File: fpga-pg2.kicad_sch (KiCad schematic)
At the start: 1 part, among them U1 XC7A15T-FTG256

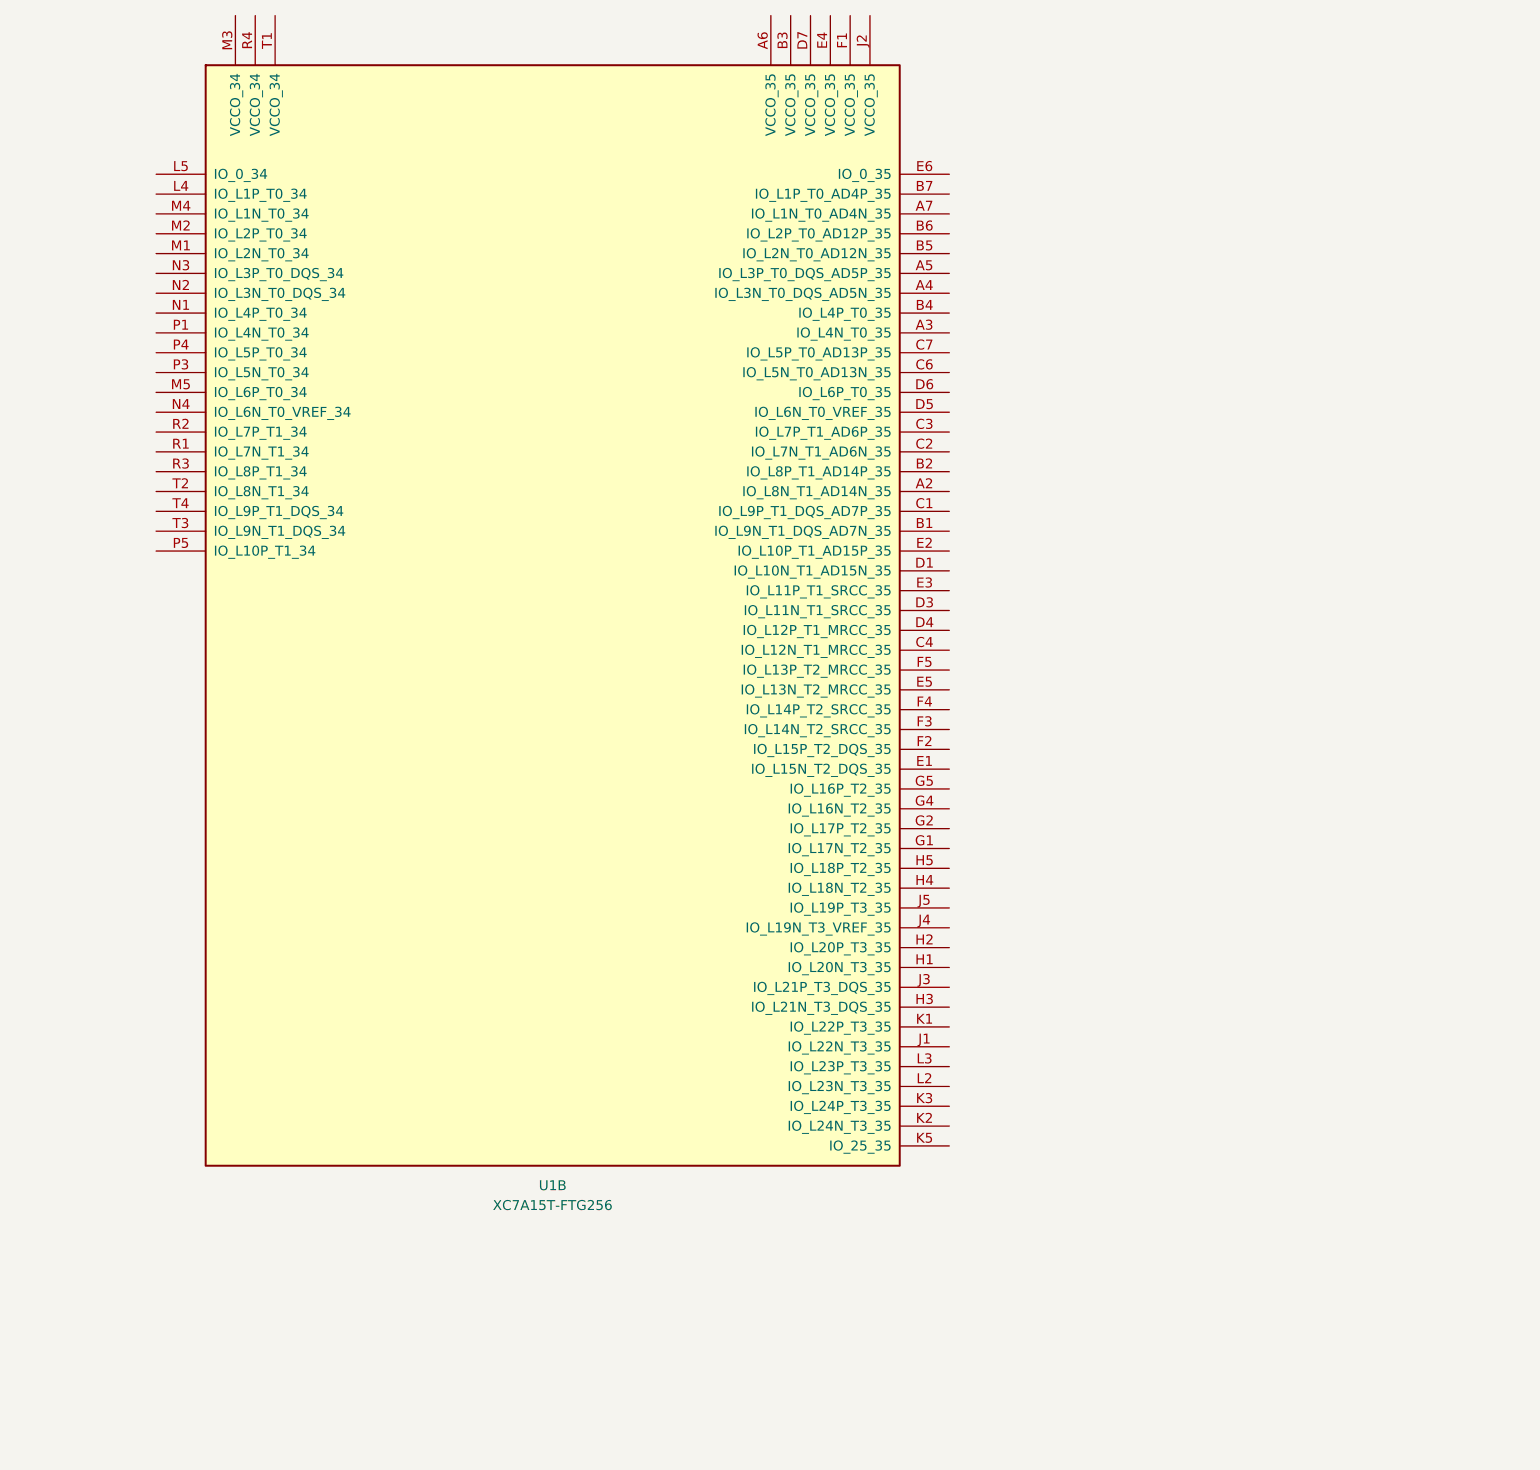
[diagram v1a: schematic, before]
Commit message: changed ftg256 to csg325, wanted xc7a12t but couldnt find
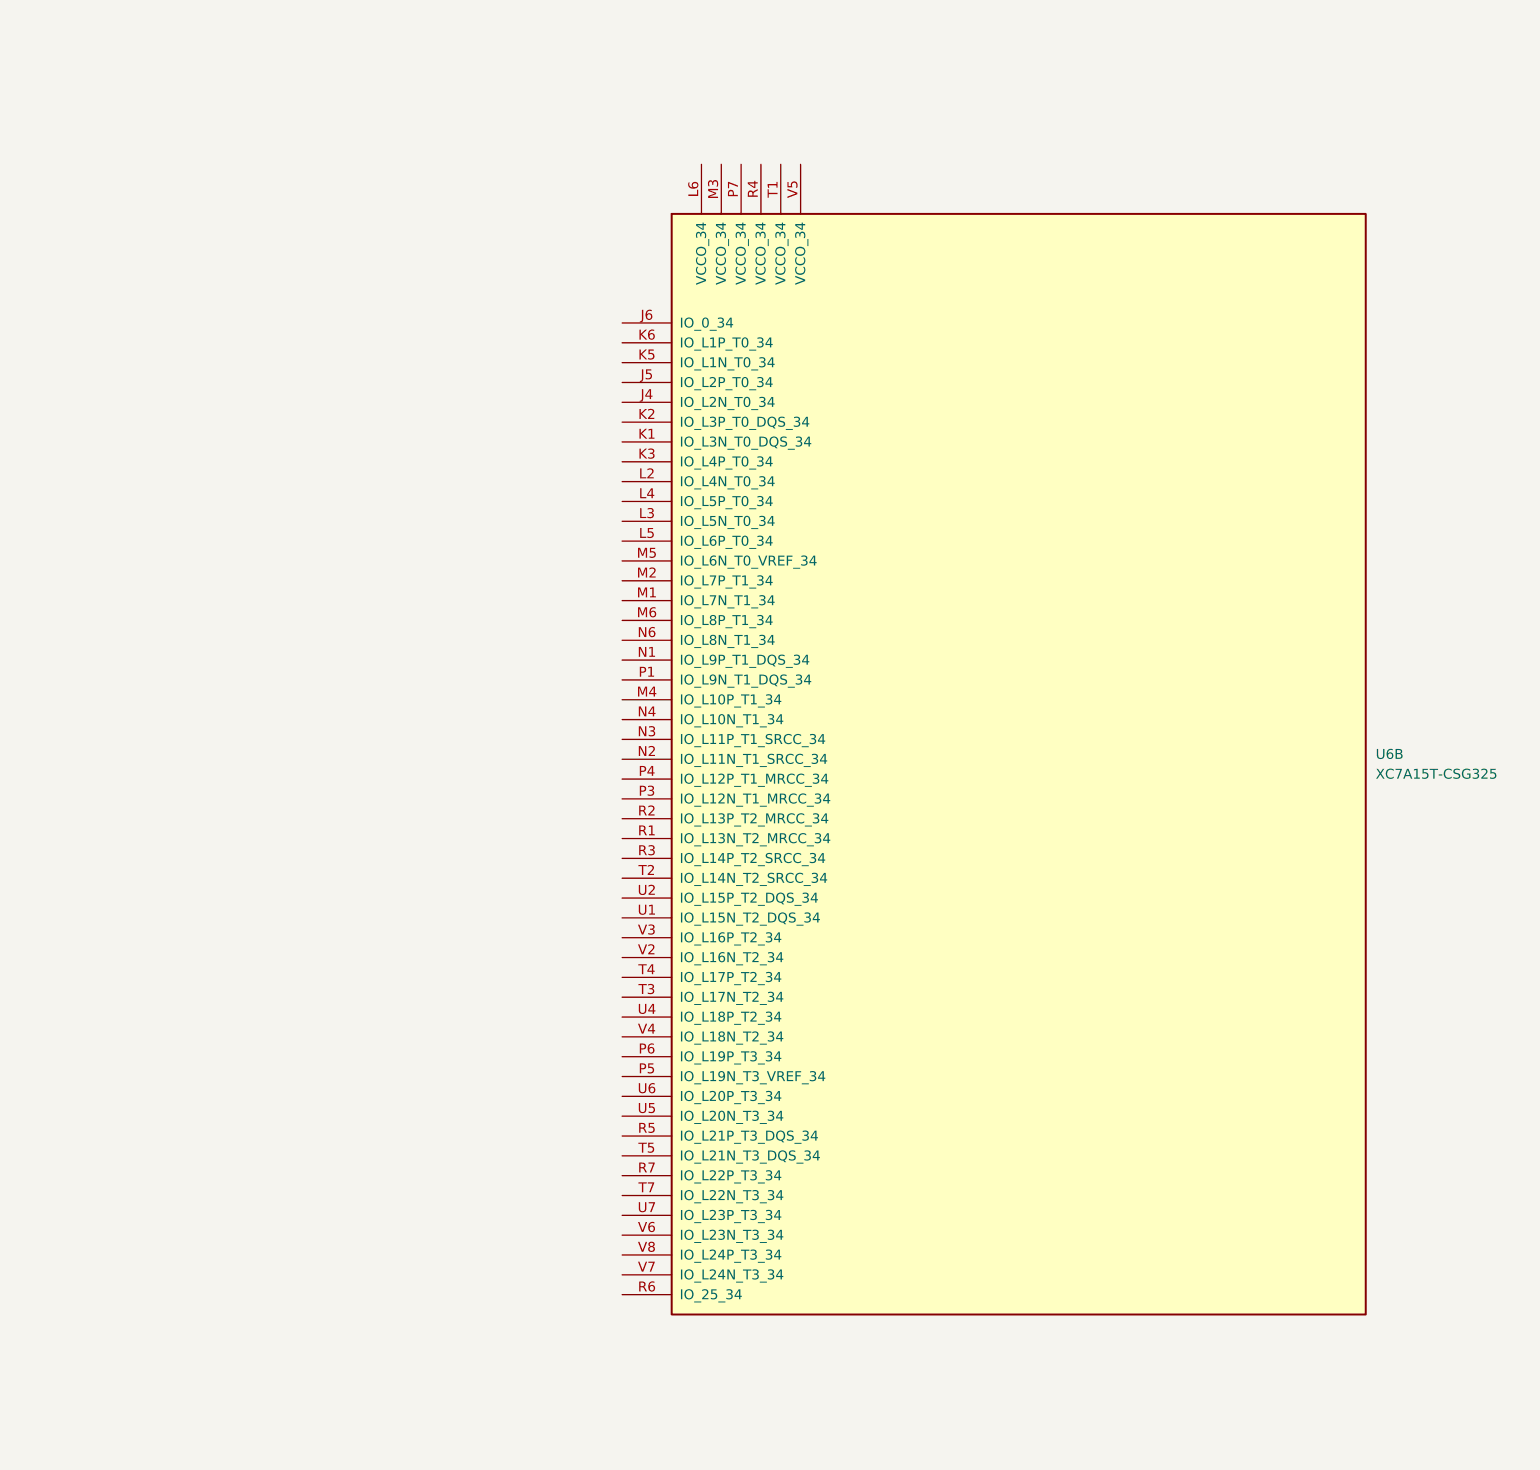
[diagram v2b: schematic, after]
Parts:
- removed U1: XC7A15T-FTG256, Package_BGA:Xilinx_FTG256, symbol FPGA_Xilinx_Artix7:XC7A15T-FTG256
- added U6: XC7A15T-CSG325, Package_BGA:Xilinx_CSG325, symbol FPGA_Xilinx_Artix7:XC7A15T-CSG325

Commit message: working on ddr3
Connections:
- net DDR3_DQ4: now reaches U6.J4 (IO_L2N_T0_34)
- net DDR3_DQ3: now reaches U6.J5 (IO_L2P_T0_34)
- net DDR3_DQ0: now reaches U6.J6 (IO_0_34)
- net DDR3_DQ6: now reaches U6.K1 (IO_L3N_T0_DQS_34)
- net DDR3_DQ5: now reaches U6.K2 (IO_L3P_T0_DQS_34)
- net DDR3_DQ7: now reaches U6.K3 (IO_L4P_T0_34)
- net DDR3_DQ2: now reaches U6.K5 (IO_L1N_T0_34)
- net DDR3_DQ1: now reaches U6.K6 (IO_L1P_T0_34)
- net DDR3_DQ8: now reaches U6.L2 (IO_L4N_T0_34)
- net DDR3_DQ10: now reaches U6.L3 (IO_L5N_T0_34)
- net DDR3_DQ9: now reaches U6.L4 (IO_L5P_T0_34)
- net DDR3_DQ11: now reaches U6.L5 (IO_L6P_T0_34)
- net DDR3_DQ14: now reaches U6.M1 (IO_L7N_T1_34)
- net DDR3_DQ13: now reaches U6.M2 (IO_L7P_T1_34)
- net DDR3_ADDR3: now reaches U6.M4 (IO_L10P_T1_34)
- net DDR3_DQ12: now reaches U6.M5 (IO_L6N_T0_VREF_34)
- net DDR3_DQ15: now reaches U6.M6 (IO_L8P_T1_34)
- net DDR3_ADDR1: now reaches U6.N1 (IO_L9P_T1_DQS_34)
- net DDR3_ADDR6: now reaches U6.N2 (IO_L11N_T1_SRCC_34)
- net DDR3_ADDR5: now reaches U6.N3 (IO_L11P_T1_SRCC_34)
- net DDR3_ADDR4: now reaches U6.N4 (IO_L10N_T1_34)
- net DDR3_ADDR0: now reaches U6.N6 (IO_L8N_T1_34)
- net DDR3_ADDR2: now reaches U6.P1 (IO_L9N_T1_DQS_34)
- net DDR3_ADDR8: now reaches U6.P3 (IO_L12N_T1_MRCC_34)
- net DDR3_ADDR7: now reaches U6.P4 (IO_L12P_T1_MRCC_34)
- net DDR3_BLOCK_ADDR2: now reaches U6.P5 (IO_L19N_T3_VREF_34)
- net DDR3_BLOCK_ADDR1: now reaches U6.P6 (IO_L19P_T3_34)
- net DDR3_ADDR10: now reaches U6.R1 (IO_L13N_T2_MRCC_34)
- net DDR3_ADDR9: now reaches U6.R2 (IO_L13P_T2_MRCC_34)
- net DDR3_ADDR11: now reaches U6.R3 (IO_L14P_T2_SRCC_34)
- net DDR3_CLK_EN: now reaches U6.R5 (IO_L21P_T3_DQS_34)
- net DDR3_ODT: now reaches U6.R7 (IO_L22P_T3_34)
- net DDR3_ADDR12: now reaches U6.T2 (IO_L14N_T2_SRCC_34)
- net DDR3_RESET#: now reaches U6.T3 (IO_L17N_T2_34)
- net DDR3_RAS#: now reaches U6.T4 (IO_L17P_T2_34)
- net DDR3_LDM: now reaches U6.T5 (IO_L21N_T3_DQS_34)
- net DDR3_UDM: now reaches U6.T7 (IO_L22N_T3_34)
- net DDR3_ADDR14: now reaches U6.U1 (IO_L15N_T2_DQS_34)
- net DDR3_ADDR13: now reaches U6.U2 (IO_L15P_T2_DQS_34)
- net DDR3_WE#: now reaches U6.U4 (IO_L18P_T2_34)
- net DDR3_CLK-: now reaches U6.U5 (IO_L20N_T3_34)
- net DDR3_CLK+: now reaches U6.U6 (IO_L20P_T3_34)
- net DDR3_LDQS+: now reaches U6.U7 (IO_L23P_T3_34)
- net DDR3_CS#: now reaches U6.V2 (IO_L16N_T2_34)
- net DDR3_CAS#: now reaches U6.V3 (IO_L16P_T2_34)
- net DDR3_BLOCK_ADDR0: now reaches U6.V4 (IO_L18N_T2_34)
- net DDR3_LDQS-: now reaches U6.V6 (IO_L23N_T3_34)
- net DDR3_UDQS-: now reaches U6.V7 (IO_L24N_T3_34)
- net DDR3_UDQS+: now reaches U6.V8 (IO_L24P_T3_34)

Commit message: working for ddr3 pcb part 2
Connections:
- net DDR3_ADDR14: now also U6.V8 (IO_L24P_T3_34); no longer U6.U1 (IO_L15N_T2_DQS_34)
- net DDR3_UDQS+: no longer U6.V8 (IO_L24P_T3_34)
- net DDR3_UDQS-: no longer U6.V7 (IO_L24N_T3_34)
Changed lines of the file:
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@@
-		)
-	)
-	(wire
-		(pts
-			(xy 208.28 224.79) (xy 223.52 224.79)
-		)
-		(stroke
-			(width 0)
-			(type default)
 		)
 	)
@@
 	(wire
 		(pts
-			(xy 208.28 227.33) (xy 223.52 227.33)
-		)
-		(stroke
-			(width 0)
-			(type default)
-		)
-	)
-	(wire
-		(pts
 			(xy 223.52 140.97) (xy 198.12 140.97)
 		)
@@
 	(wire
 		(pts
-			(xy 198.12 181.61) (xy 223.52 181.61)
-		)
-		(stroke
-			(width 0)
-			(type default)
-		)
-	)
-	(wire
-		(pts
 			(xy 223.52 110.49) (xy 198.12 110.49)
 		)
@@
 	(wire
 		(pts
+			(xy 198.12 224.79) (xy 223.52 224.79)
+		)
+		(stroke
+			(width 0)
+			(type default)
+		)
+	)
+	(wire
+		(pts
 			(xy 198.12 153.67) (xy 223.52 153.67)
 		)
@@
 	(wire
 		(pts
+			(xy 207.01 248.92) (xy 222.25 248.92)
+		)
+		(stroke
+			(width 0)
+			(type default)
+		)
+	)
+	(wire
+		(pts
 			(xy 198.12 148.59) (xy 223.52 148.59)
 		)
@@
 		(pts
 			(xy 195.58 151.13) (xy 195.58 153.67)
+		)
+		(stroke
+			(width 0)
+			(type default)
+		)
+	)
+	(wire
+		(pts
+			(xy 207.01 246.38) (xy 222.25 246.38)
 		)
 		(stroke
@@
 		)
 	)
-	(label "DDR3_ADDR14"
-		(at 208.28 181.61 0)
-		(effects
-			(font
-				(size 1.27 1.27)
-			)
-			(justify left bottom)
-		)
-	)
 	(label "DDR3_DQ11"
 		(at 208.28 133.35 0)
@@
 		)
 	)
-	(label "DDR3_UDQS-"
-		(at 208.28 227.33 0)
-		(effects
-			(font
-				(size 1.27 1.27)
-			)
-			(justify left bottom)
-		)
-	)
 	(label "DDR3_DQ14"
 		(at 208.28 140.97 0)
@@
 		)
 	)
+	(label "DDR3_ADDR14"
+		(at 208.28 224.79 0)
+		(effects
+			(font
+				(size 1.27 1.27)
+			)
+			(justify left bottom)
+		)
+	)
 	(label "DDR3_ADDR2"
 		(at 208.28 151.13 0)
@@
 	)
 	(label "DDR3_UDQS+"
-		(at 208.28 224.79 0)
+		(at 207.01 246.38 0)
 		(effects
 			(font
@@
 		)
 	)
+	(label "DDR3_UDQS-"
+		(at 207.01 248.92 0)
+		(effects
+			(font
+				(size 1.27 1.27)
+			)
+			(justify left bottom)
+		)
+	)
 	(label "DDR3_CS#"
 		(at 208.28 186.69 0)
@@
 		)
 	)
+	(hierarchical_label "DDR3_UDQS+"
+		(shape bidirectional)
+		(at 207.01 246.38 180)
+		(effects
+			(font
+				(size 1.27 1.27)
+			)
+			(justify right)
+		)
+	)
 	(hierarchical_label "DDR3_WE#"
 		(shape bidirectional)
@@
 		)
 	)
+	(hierarchical_label "DDR3_LDQS+"
+		(shape bidirectional)
+		(at 208.28 219.71 180)
+		(effects
+			(font
+				(size 1.27 1.27)
+			)
+			(justify right)
+		)
+	)
+	(hierarchical_label "DDR3_ODT"
+		(shape bidirectional)
+		(at 208.28 214.63 180)
+		(effects
+			(font
+				(size 1.27 1.27)
+			)
+			(justify right)
+		)
+	)
 	(hierarchical_label "DDR3_UDQS-"
 		(shape bidirectional)
-		(at 208.28 227.33 180)
-		(effects
-			(font
-				(size 1.27 1.27)
-			)
-			(justify right)
-		)
-	)
-	(hierarchical_label "DDR3_LDQS+"
-		(shape bidirectional)
-		(at 208.28 219.71 180)
-		(effects
-			(font
-				(size 1.27 1.27)
-			)
-			(justify right)
-		)
-	)
-	(hierarchical_label "DDR3_ODT"
-		(shape bidirectional)
-		(at 208.28 214.63 180)
+		(at 207.01 248.92 180)
 		(effects
 			(font
@@
 		(effects
 			(font
-				(size 1.27 1.27)
-			)
-			(justify right)
-		)
-	)
-	(hierarchical_label "DDR3_UDQS+"
-		(shape bidirectional)
-		(at 208.28 224.79 180)
-		(effects
-			(font

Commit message: more ddr3, rules and stuff
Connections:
- net DDR3_ADDR0: now also U6.U5 (IO_L20N_T3_34); no longer U6.N6 (IO_L8N_T1_34)
- net DDR3_ADDR1: now also U6.U1 (IO_L15N_T2_DQS_34); no longer U6.N1 (IO_L9P_T1_DQS_34)
- net DDR3_ADDR10: now also U6.P3 (IO_L12N_T1_MRCC_34); no longer U6.R1 (IO_L13N_T2_MRCC_34)
- net DDR3_ADDR11: now also U6.U2 (IO_L15P_T2_DQS_34); no longer U6.R3 (IO_L14P_T2_SRCC_34)
- net DDR3_ADDR12: now also U6.R3 (IO_L14P_T2_SRCC_34); no longer U6.T2 (IO_L14N_T2_SRCC_34)
- net DDR3_ADDR13: no longer U6.U2 (IO_L15P_T2_DQS_34)
- net DDR3_ADDR14: now also U6.V2 (IO_L16N_T2_34); no longer U6.V8 (IO_L24P_T3_34)
- net DDR3_ADDR2: now also U6.V6 (IO_L23N_T3_34); no longer U6.P1 (IO_L9N_T1_DQS_34)
- net DDR3_ADDR3: now also U6.V4 (IO_L18N_T2_34); no longer U6.M4 (IO_L10P_T1_34)
- net DDR3_ADDR4: now also U6.T2 (IO_L14N_T2_SRCC_34); no longer U6.N4 (IO_L10N_T1_34)
- net DDR3_ADDR5: now also U6.U6 (IO_L20P_T3_34); no longer U6.N3 (IO_L11P_T1_SRCC_34)
- net DDR3_ADDR6: now also U6.T3 (IO_L17N_T2_34); no longer U6.N2 (IO_L11N_T1_SRCC_34)
- net DDR3_ADDR7: now also U6.V7 (IO_L24N_T3_34); no longer U6.P4 (IO_L12P_T1_MRCC_34)
- net DDR3_ADDR8: now also U6.T4 (IO_L17P_T2_34); no longer U6.P3 (IO_L12N_T1_MRCC_34)
- net DDR3_ADDR9: now also U6.V8 (IO_L24P_T3_34); no longer U6.R2 (IO_L13P_T2_MRCC_34)
- net DDR3_BLOCK_ADDR0: now also U6.V3 (IO_L16P_T2_34); no longer U6.V4 (IO_L18N_T2_34)
- net DDR3_BLOCK_ADDR1: now also U6.R2 (IO_L13P_T2_MRCC_34); no longer U6.P6 (IO_L19P_T3_34)
- net DDR3_BLOCK_ADDR2: no longer U6.P5 (IO_L19N_T3_VREF_34)
- net DDR3_CAS#: no longer U6.V3 (IO_L16P_T2_34)
- net DDR3_CLK+: no longer U6.U6 (IO_L20P_T3_34)
- net DDR3_CLK-: no longer U6.U5 (IO_L20N_T3_34)
- net DDR3_CS#: no longer U6.V2 (IO_L16N_T2_34)
- net DDR3_LDQS-: no longer U6.V6 (IO_L23N_T3_34)
- net DDR3_RAS#: no longer U6.T4 (IO_L17P_T2_34)
- net DDR3_RESET#: no longer U6.T3 (IO_L17N_T2_34)
- net DDR3_WE#: no longer U6.U4 (IO_L18P_T2_34)

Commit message: wip rickard
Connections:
- net DDR3_ADDR13: now also U6.N1 (IO_L9P_T1_DQS_34)
- net DDR3_BLOCK_ADDR2: now also U6.U4 (IO_L18P_T2_34)
- net DDR3_CAS#: now also U6.P1 (IO_L9N_T1_DQS_34)
- net DDR3_CLK+: now also U6.P4 (IO_L12P_T1_MRCC_34)
- net DDR3_CLK-: now also U6.N2 (IO_L11N_T1_SRCC_34)
- net DDR3_CS#: now also U6.N3 (IO_L11P_T1_SRCC_34)
- net DDR3_DQ0: now also U6.K5 (IO_L1N_T0_34); no longer U6.J6 (IO_0_34)
- net DDR3_DQ1: now also U6.K1 (IO_L3N_T0_DQS_34); no longer U6.K6 (IO_L1P_T0_34)
- net DDR3_DQ10: now also U6.K2 (IO_L3P_T0_DQS_34); no longer U6.L3 (IO_L5N_T0_34)
- net DDR3_DQ11: now also U6.K6 (IO_L1P_T0_34); no longer U6.L5 (IO_L6P_T0_34)
- net DDR3_DQ12: now also U6.J6 (IO_0_34); no longer U6.M5 (IO_L6N_T0_VREF_34)
- net DDR3_DQ13: now also U6.J4 (IO_L2N_T0_34); no longer U6.M2 (IO_L7P_T1_34)
- net DDR3_DQ14: now also U6.K3 (IO_L4P_T0_34); no longer U6.M1 (IO_L7N_T1_34)
- net DDR3_DQ15: now also U6.J5 (IO_L2P_T0_34); no longer U6.M6 (IO_L8P_T1_34)
- net DDR3_DQ2: now also U6.L5 (IO_L6P_T0_34); no longer U6.K5 (IO_L1N_T0_34)
- net DDR3_DQ3: now also U6.L4 (IO_L5P_T0_34); no longer U6.J5 (IO_L2P_T0_34)
- net DDR3_DQ4: now also U6.M6 (IO_L8P_T1_34); no longer U6.J4 (IO_L2N_T0_34)
- net DDR3_DQ5: now also U6.M5 (IO_L6N_T0_VREF_34); no longer U6.K2 (IO_L3P_T0_DQS_34)
- net DDR3_DQ6: now also U6.L3 (IO_L5N_T0_34); no longer U6.K1 (IO_L3N_T0_DQS_34)
- net DDR3_DQ7: now also U6.M1 (IO_L7N_T1_34); no longer U6.K3 (IO_L4P_T0_34)
- net DDR3_DQ9: now also U6.M2 (IO_L7P_T1_34); no longer U6.L4 (IO_L5P_T0_34)
- net DDR3_LDQS-: now also U6.R1 (IO_L13N_T2_MRCC_34)
- net DDR3_RAS#: now also U6.N6 (IO_L8N_T1_34)
- net DDR3_RESET#: now also U6.M4 (IO_L10P_T1_34)
- net DDR3_UDQS+: now also U6.P6 (IO_L19P_T3_34)
- net DDR3_UDQS-: now also U6.P5 (IO_L19N_T3_VREF_34)
- net DDR3_WE#: now also U6.N4 (IO_L10N_T1_34)
